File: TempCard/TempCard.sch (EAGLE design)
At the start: 28 parts, among them Q1 MOSFET-NCHANNELBSS138, Q2 MOSFET-NCHANNELBSS138, Q3 MOSFET-NCHANNELBSS138, Q4 MOSFET-NCHANNELBSS138, U1 MIC5219 3.3V, U3 MAG3110, U4 ATTINY85-20SU

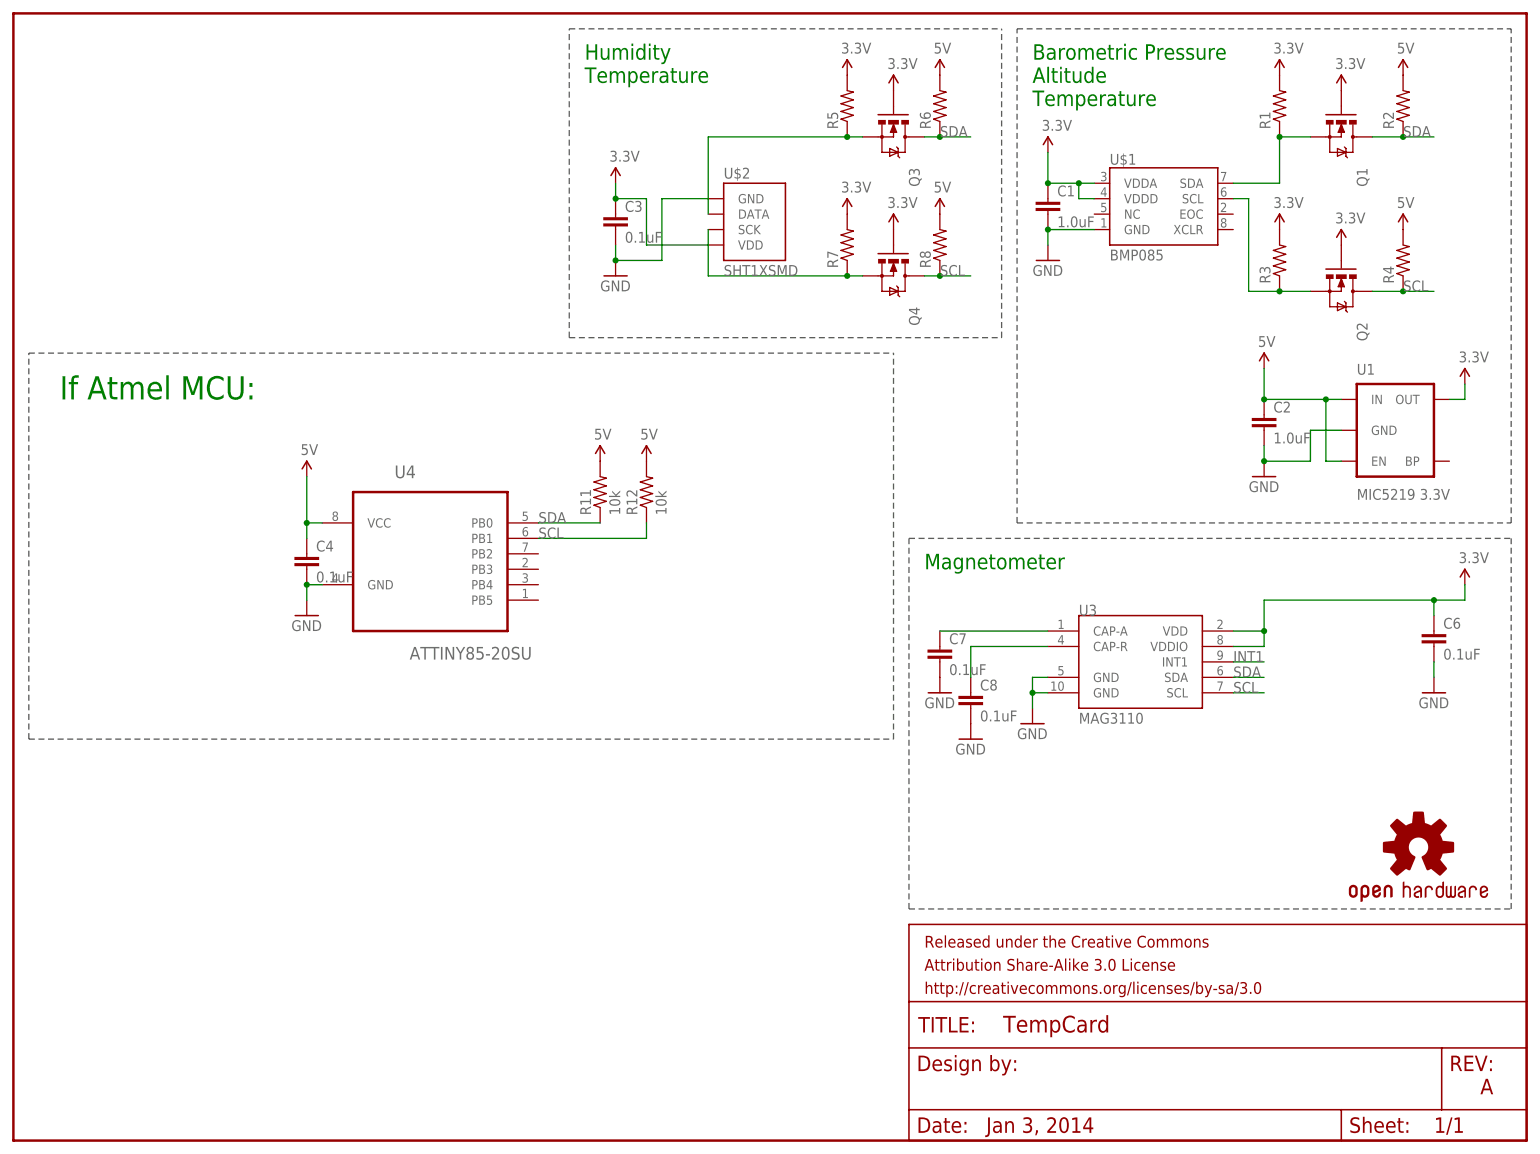
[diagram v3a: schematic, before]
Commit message: Final Hardware Selected
HTU21D, MAG3110, BMP180. Still room in the future for adding LCD screen as well as other functionality in different series.

Signed-off-by: Scott Lerner <scottphiliplerner@gmail.com>
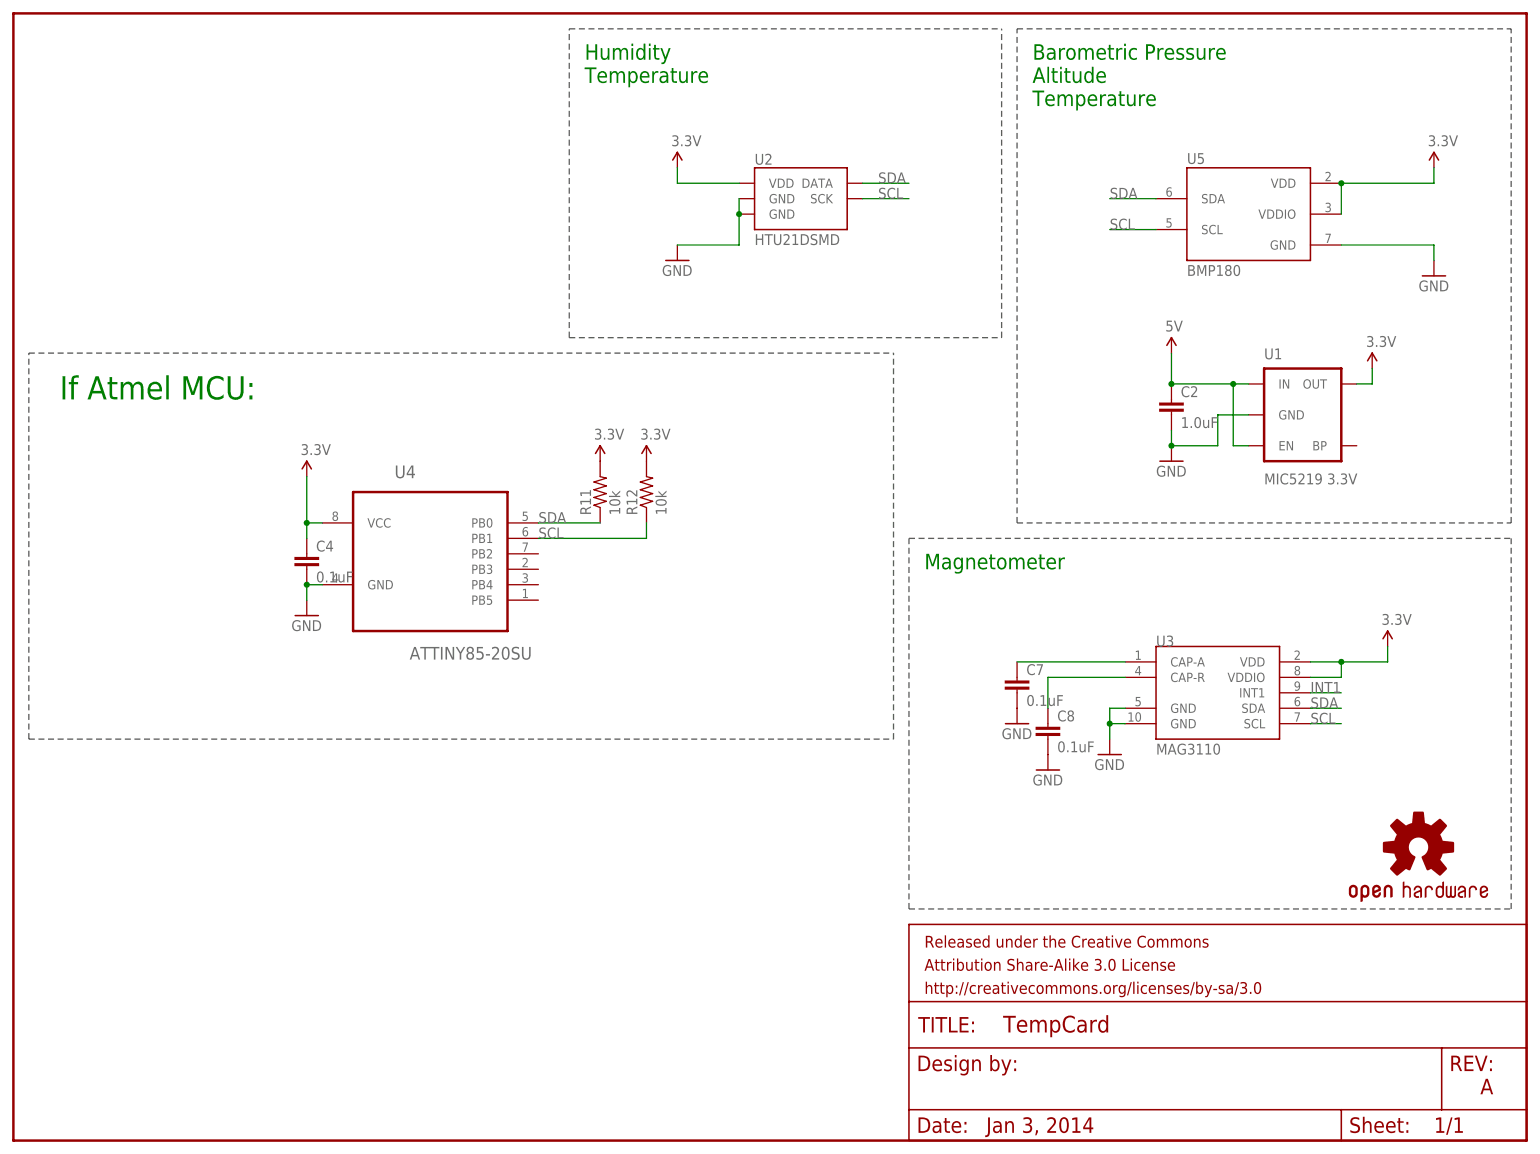
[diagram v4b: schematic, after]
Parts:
- removed C1: 1.0uF, SparkFun-Capacitors:1.0UF-25V-+80/-20(0805)
- removed C3: 0.1uF, SparkFun-Capacitors:1.0UF-25V-+80/-20(0805)
- removed C6: 0.1uF, SparkFun-Passives:CAP0402-CAP
- removed Q1, Q2, Q3, Q4: MOSFET-NCHANNELBSS138, SparkFun-DiscreteSemi:MOSFET-NCHANNELBSS138
- removed R1, R2, R3, R4, R5, R6, R7, R8: (no value), SparkFun-Resistors:RESISTOR0805-RES
- removed U$1: BMP085, SparkFun-Sensors:BMP085
- removed U$2: SHT1XSMD, SparkFun-Sensors:SHT1XSMD
- added U2: HTU21DSMD, SparkFun-Sensors:HTU21DSMD
- added U5: BMP180, SparkFun-Sensors:BMP180
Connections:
- removed net N$1: Q1.S, R1.1, U$1.SDA
- removed net N$2: Q2.S, R3.1, U$1.SCL
- removed net N$5: Q4.S, R7.1, U$2.SCK
- removed net N$9: Q3.S, R5.1, U$2.DATA
- net 3.3V: now also C4.1, R11.2, R12.2, U2.VDD, U4.VCC, U5.VDD, U5.VDDIO; no longer C1.1, C3.1, C6.1, Q1.G, Q2.G, Q3.G, Q4.G, R1.2, R3.2, R5.2, R7.2, U$1.VDDA, U$1.VDDD, U$2.VDD
- net 5V: no longer C4.1, R11.2, R12.2, R2.2, R4.2, R6.2, R8.2, U4.VCC
- net GND: now also U2.GND@2, U2.GND@7, U5.GND; no longer C1.2, C3.2, C6.2, U$1.GND, U$2.GND
- net SCL: no longer Q2.D, Q4.D, R4.1, R8.1
- net SDA: no longer Q1.D, Q3.D, R2.1, R6.1
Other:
- moved on the sheet: C2, C7, C8, U1, U3
